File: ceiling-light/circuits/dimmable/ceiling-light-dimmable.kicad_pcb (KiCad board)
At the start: 2 copper layers, 37 parts, among them J1 Screw_Terminal_01x03, J2 Screw_Terminal_01x02, J3 Conn_01x07, J4 Conn_01x01, J5 Conn_01x01, Q2 IRF840, Q3 IRF840, Q4 KSP44, SW1 SW_Push, SW2 SW_Push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

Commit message: work on dimmable schematic
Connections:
- U4 pad 10: Net-(U4-Pad10) -> Net-(R13-Pad2)
- U4 pad 6: Net-(U4-Pad6) -> GND
- U4 pad 7: Net-(U4-Pad7) -> /DIM_MODE
- U4 pad 8: Net-(U4-Pad8) -> +5V
- U4 pad 9: Net-(U4-Pad9) -> /DIMCN
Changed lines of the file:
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@@
     (zones 0)
     (modules 37)
-    (nets 63)
+    (nets 58)
   )
   (page User 129.997 180.01)
@@
   (net 56 /DIMCN)
   (net 57 /DIM_MODE)
-  (net 58 "Net-(U4-Pad10)")
-  (net 59 "Net-(U4-Pad9)")
-  (net 60 "Net-(U4-Pad8)")
-  (net 61 "Net-(U4-Pad7)")
-  (net 62 "Net-(U4-Pad6)")
   (net_class Default "This is the default net class."
     (clearance 0.2)
@@
     (add_net "Net-(SW1-Pad1)")
     (add_net "Net-(SW2-Pad2)")
-    (add_net "Net-(U4-Pad10)")
-    (add_net "Net-(U4-Pad6)")
-    (add_net "Net-(U4-Pad7)")
-    (add_net "Net-(U4-Pad8)")
-    (add_net "Net-(U4-Pad9)")
     (add_net "Net-(U6-Pad10)")
     (add_net "Net-(U6-Pad11)")
@@
     (fp_circle (center -1.7 1.2) (end -1.45 1.2) (layer F.SilkS) (width 0.5))
     (pad 10 smd rect (at -2 -2.8) (size 0.65 1.75) (layers F.Cu F.Paste F.Mask)
-      (net 58 "Net-(U4-Pad10)"))
+      (net 19 "Net-(R13-Pad2)"))
     (pad 9 smd rect (at -1 -2.8) (size 0.65 1.75) (layers F.Cu F.Paste F.Mask)
-      (net 59 "Net-(U4-Pad9)"))
+      (net 56 /DIMCN))
     (pad 8 smd rect (at 0 -2.8) (size 0.65 1.75) (layers F.Cu F.Paste F.Mask)
-      (net 60 "Net-(U4-Pad8)"))
+      (net 52 +5V))
     (pad 7 smd rect (at 1 -2.8) (size 0.65 1.75) (layers F.Cu F.Paste F.Mask)
-      (net 61 "Net-(U4-Pad7)"))
+      (net 57 /DIM_MODE))
     (pad 6 smd rect (at 2 -2.8) (size 0.65 1.75) (layers F.Cu F.Paste F.Mask)
-      (net 62 "Net-(U4-Pad6)"))
+      (net 14 GND))
     (pad 5 smd rect (at 2 2.8) (size 0.65 1.75) (layers F.Cu F.Paste F.Mask)
       (net 53 "Net-(C3-Pad1)"))

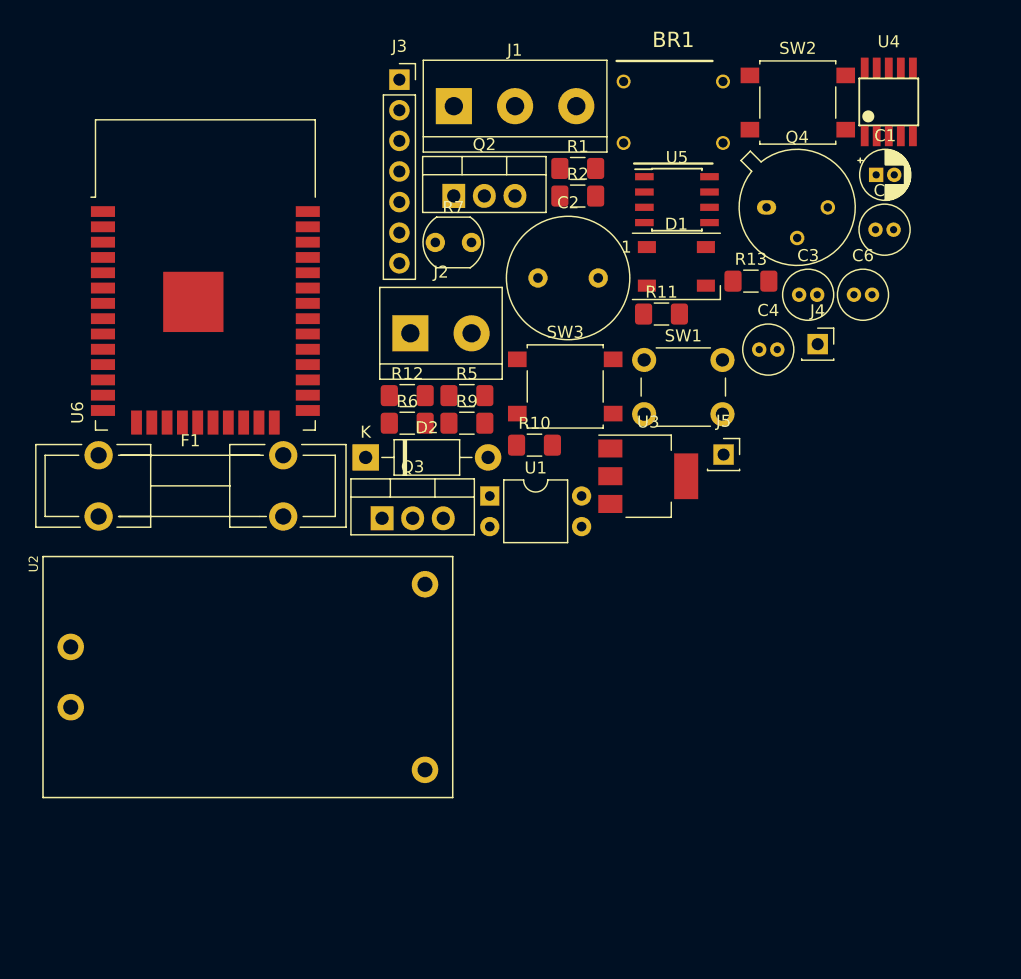
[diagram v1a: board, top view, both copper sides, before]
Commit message: PCB layout for v1.1.0 through hole prototype
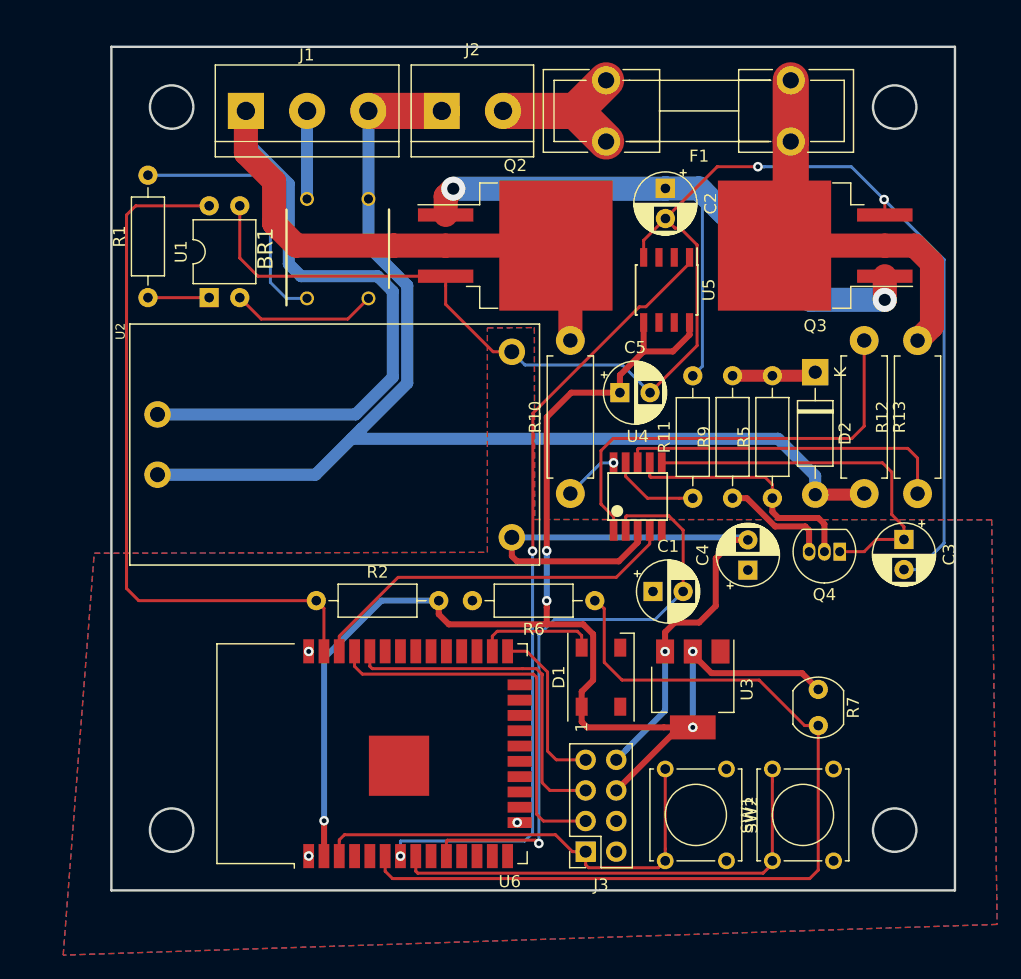
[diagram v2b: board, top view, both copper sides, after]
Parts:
- removed C6: 0.1µF, Capacitor_THT:C_Radial_D4.0mm_H5.0mm_P1.50mm
- removed J4, J5: Conn_01x01, Connector_PinSocket_2.54mm:PinSocket_1x01_P2.54mm_Vertical
- removed SW3: SW_Push, Button_Switch_SMD:SW_SPST_B3S-1000
- C1: value 1µF -> 100nF; footprint Capacitor_THT:CP_Radial_D4.0mm_P1.50mm -> Capacitor_THT:CP_Radial_D5.0mm_P2.50mm
- C2: footprint Capacitor_THT:C_Radial_D10.0mm_H12.5mm_P5.00mm -> Capacitor_THT:CP_Radial_D5.0mm_P2.50mm
- C3: value 22nF -> 4µ7; footprint Capacitor_THT:C_Radial_D4.0mm_H5.0mm_P1.50mm -> Capacitor_THT:CP_Radial_D5.0mm_P2.50mm
- C4: footprint Capacitor_THT:C_Radial_D4.0mm_H5.0mm_P1.50mm -> Capacitor_THT:CP_Radial_D5.0mm_P2.50mm
- C5: value 0.1µF -> 0.1µ; footprint Capacitor_THT:C_Radial_D4.0mm_H5.0mm_P1.50mm -> Capacitor_THT:CP_Radial_D5.0mm_P2.50mm
- J3: value Conn_01x07 -> Conn_02x04_Counter_Clockwise; footprint Connector_PinSocket_2.54mm:PinSocket_1x07_P2.54mm_Vertical -> Connector_PinSocket_2.54mm:PinSocket_2x04_P2.54mm_Vertical
- Q2, Q3: footprint Package_TO_SOT_THT:TO-220-3_Vertical -> Package_TO_SOT_SMD:TO-263-3_TabPin2
- Q4: footprint Package_TO_SOT_THT:TO-39-3 -> Package_TO_SOT_THT:TO-92_Inline
- R1, R11, R2, R5, R6, R9: footprint Resistor_SMD:R_1206_3216Metric_Pad1.42x1.75mm_HandSolder -> Resistor_THT:R_Axial_DIN0207_L6.3mm_D2.5mm_P10.16mm_Horizontal
- R10, R12, R13: value 2M -> 2M2; footprint Resistor_SMD:R_1206_3216Metric_Pad1.42x1.75mm_HandSolder -> Resistor_THT:R_Axial_DIN0411_L9.9mm_D3.6mm_P12.70mm_Horizontal
- SW1: footprint Button_Switch_THT:SW_PUSH_6mm -> Button_Switch_THT:SW_Tactile_Straight_KSA0Axx1LFTR
- SW2: footprint Button_Switch_SMD:SW_SPST_B3S-1000 -> Button_Switch_THT:SW_Tactile_Straight_KSA0Axx1LFTR
- moved J3 65.9 mm to (67.8, 91.7), turned to 180 degrees
- moved F1 63.1 mm to (84.8, 32.8), turned to 180 degrees
- moved SW2 55.6 mm to (79.5, 84.8), turned to 270 degrees
- moved R7 48.8 mm to (87.1, 78.2), turned to 270 degrees
- moved R12 43.1 mm to (95.4, 62.0), turned to 90 degrees
- moved SW1 42.9 mm to (83.3, 92.5), turned to 90 degrees
- moved Q3 42.5 mm to (86.9, 41.4), turned to 180 degrees
- moved U6 40.4 mm to (53.1, 83.6), turned to 90 degrees
- moved R2 40.0 mm to (45.5, 70.9)
- moved C1 39.2 mm to (73.4, 70.1)
- moved U4 38.8 mm to (72.1, 62.2)
- moved D2 38.0 mm to (86.9, 51.9), turned to 270 degrees
- moved R1 37.2 mm to (31.5, 45.7), turned to 90 degrees
- moved D1 34.7 mm to (69.1, 77.2), turned to 90 degrees
- moved BR1 30.1 mm to (47.3, 41.6), turned to 90 degrees
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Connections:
- net /ESP_TX renamed /ESP_TXD0
- net /M1_IN renamed /L_M1
- net /M2_IN renamed /L_M2
- net Net-(U6-Pad11) renamed /ESP_GPIO_26
- net Net-(U6-Pad12) renamed /ESP_GPIO_27
- net Net-(U6-Pad13) renamed /ESP_GPIO_14
- net Net-(U6-Pad14) renamed /ESP_GPIO_12
- net Net-(U6-Pad16) renamed /ESP_GPIO_13
- net Net-(U6-Pad23) renamed /ESP_GPIO_15
- net Net-(U6-Pad24) renamed /ESP_GPIO_02
- net Net-(U6-Pad27) renamed /ESP_GPIO_16
- net Net-(U6-Pad28) renamed /ESP_GPIO_17
- net Net-(U6-Pad29) renamed /ESP_GPIO_05
- net Net-(U6-Pad30) renamed /ESP_GPIO_18
- net Net-(U6-Pad31) renamed /ESP_GPIO_19
- net Net-(U6-Pad33) renamed /ESP_GPIO_21
- C1 pad 1: /MAINS_SENSE -> GND
- C1 pad 2: GND -> /ESP_GPIO_25
- D1 pad 4: /STATUS_LED -> /ESP_GPIO_04
- J3 pad 1: +5V -> /ESP_EN
- J3 pad 4: /ESP_RX -> GND
- J3 pad 5: /ESP_FLASH -> /ESP_RXD0
- J3 pad 7: GND -> /ESP_GPIO_00
- R13 pad 1: /N_MAIN -> Net-(R13-Pad1)
- R13 pad 2: Net-(R13-Pad2) -> /N_MAIN
- R2 pad 1: /MAINS_SENSE -> /ESP_GPIO_23
- R6 pad 1: /LIGHT_SENSE -> /ESP_GPIO_34
- R7 pad 2: /LIGHT_SENSE -> /ESP_GPIO_34
- SW2 pad 2: Net-(SW2-Pad2) -> /ESP_EN
- U1 pad 4: /MAINS_SENSE -> /ESP_GPIO_23
- U4 pad 1: Net-(R10-Pad1) -> Net-(R13-Pad1)
- U4 pad 10: Net-(R13-Pad2) -> Net-(R10-Pad1)
- U4 pad 2: Net-(R11-Pad1) -> /ESP_GPIO_25
- U4 pad 3: Net-(R12-Pad1) -> +5V
- U4 pad 4: Net-(Q4-Pad2) -> /ESP_GPIO_22
- U4 pad 5: Net-(C3-Pad1) -> GND
- U4 pad 6: GND -> Net-(C3-Pad1)
- U4 pad 7: /DIM_MODE -> Net-(Q4-Pad2)
- U4 pad 8: +5V -> Net-(R12-Pad1)
- U4 pad 9: /DIMCN -> Net-(R11-Pad1)
- U5 pad 1: /TEMP_SENSE -> /ESP_GPIO_35
- U6 pad 10: Net-(U6-Pad10) -> /ESP_GPIO_25
- U6 pad 25: /ESP_FLASH -> /ESP_GPIO_00
- U6 pad 26: Net-(U6-Pad26) -> /ESP_GPIO_04
- U6 pad 3: Net-(SW2-Pad2) -> /ESP_EN
- U6 pad 34: /ESP_RX -> /ESP_RXD0
- U6 pad 36: Net-(U6-Pad36) -> /ESP_GPIO_22
- U6 pad 37: Net-(U6-Pad37) -> /ESP_GPIO_23
- U6 pad 4: /TEMP_SENSE -> /ESP_SENSOR_VP
- U6 pad 5: /LIGHT_SENSE -> /ESP_SENSOR_VN
- U6 pad 6: /MAINS_SENSE -> /ESP_GPIO_34
- U6 pad 7: Net-(U6-Pad7) -> /ESP_GPIO_35
- U6 pad 9: /STATUS_LED -> /ESP_GPIO_33
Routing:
- net GND: track 0.00 -> 123.5 mm, vias 0 -> 5
- net +3V3: track 0.00 -> 122.5 mm, vias 0 -> 5
- net /N_MAIN: track 0.00 -> 99.3 mm
- net /L_M2: track 0.00 -> 94.5 mm
- net /ESP_GPIO_34: track 0.00 -> 75.2 mm
- net /ESP_GPIO_35: track 0.00 -> 66.0 mm, vias 0 -> 2
- net Net-(C2-Pad1): track 0.00 -> 61.4 mm, vias 0 -> 2
- net +5V: track 0.00 -> 58.9 mm, vias 0 -> 1
- net /ESP_GPIO_23: track 0.00 -> 58.8 mm
- net /ESP_GPIO_25: track 0.00 -> 51.3 mm, vias 0 -> 1
- net Net-(SW1-Pad1): track 0.00 -> 39.1 mm
- net /ESP_EN: track 0.00 -> 38.2 mm
- net Net-(R13-Pad1): track 0.00 -> 36.8 mm
- net /L_OUT: track 0.00 -> 34.9 mm
- net /ESP_TXD0: track 0.00 -> 32.4 mm
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- added copper zone on B.Cu, net GND
- added copper zone on F.Cu, net GND
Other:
- board outline added: 70 x 70 mm
